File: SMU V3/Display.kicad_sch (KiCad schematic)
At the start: 3 parts, among them U1301 Display

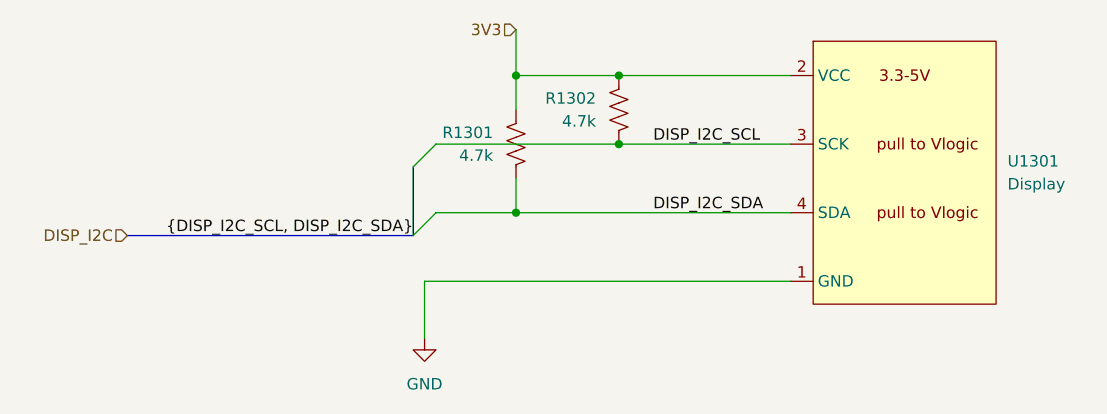
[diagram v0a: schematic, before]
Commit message: improved V3
added uart/spi test points and status leds
removed main 3v3 ldo
added silkscreen
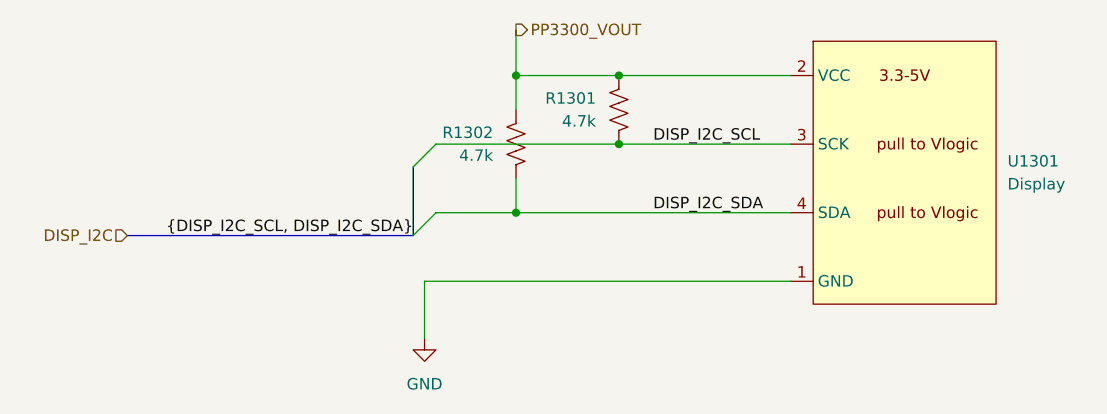
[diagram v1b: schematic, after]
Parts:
- renumbered R1302 to R1301, R1301 to R1302
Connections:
- net 3V3 renamed PP3300_VOUT
